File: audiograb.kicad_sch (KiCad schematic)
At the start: 4 parts, among them J2 USB_C_Receptacle_USB2.0_16P

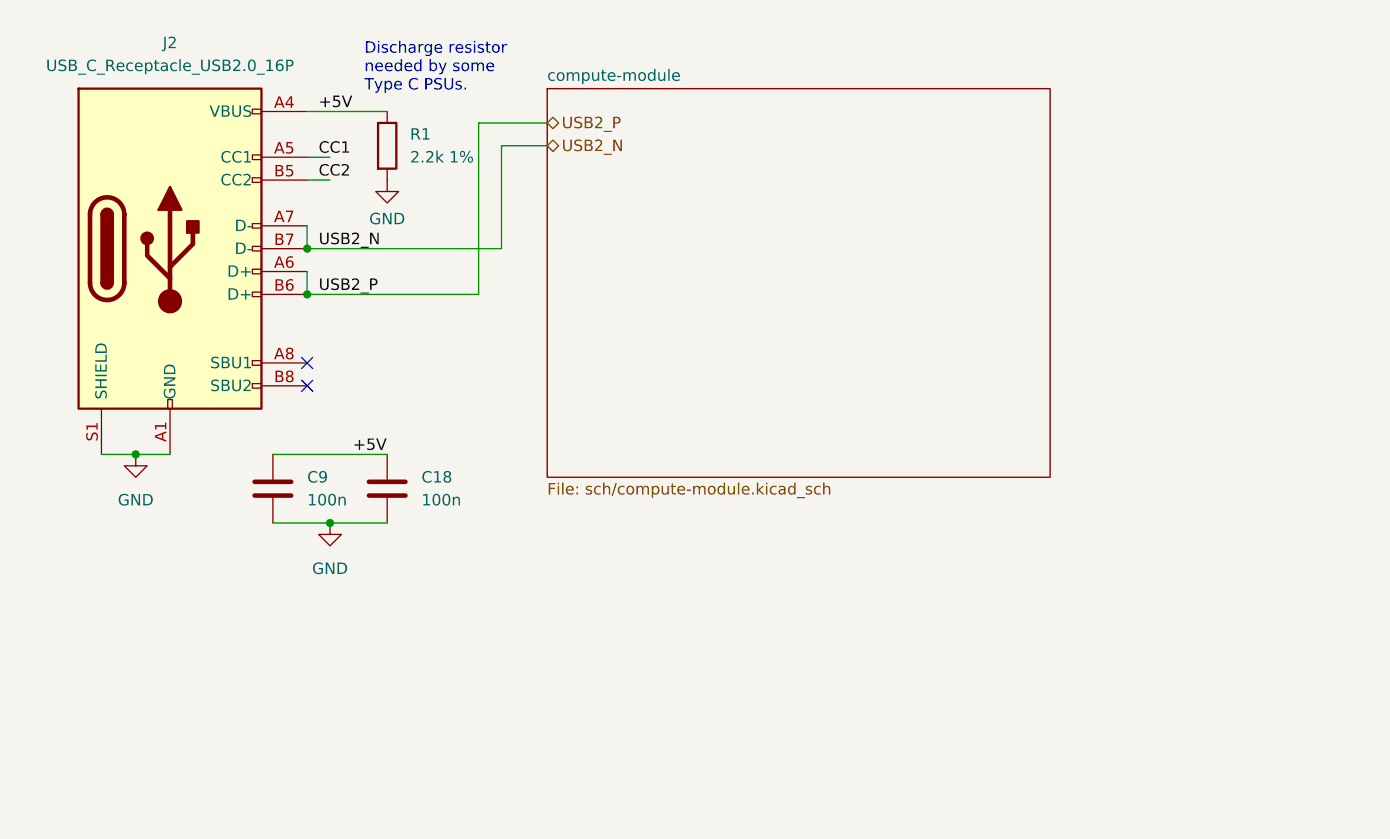
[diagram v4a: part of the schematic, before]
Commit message: compute module: added GPIO header, power, battery, among others
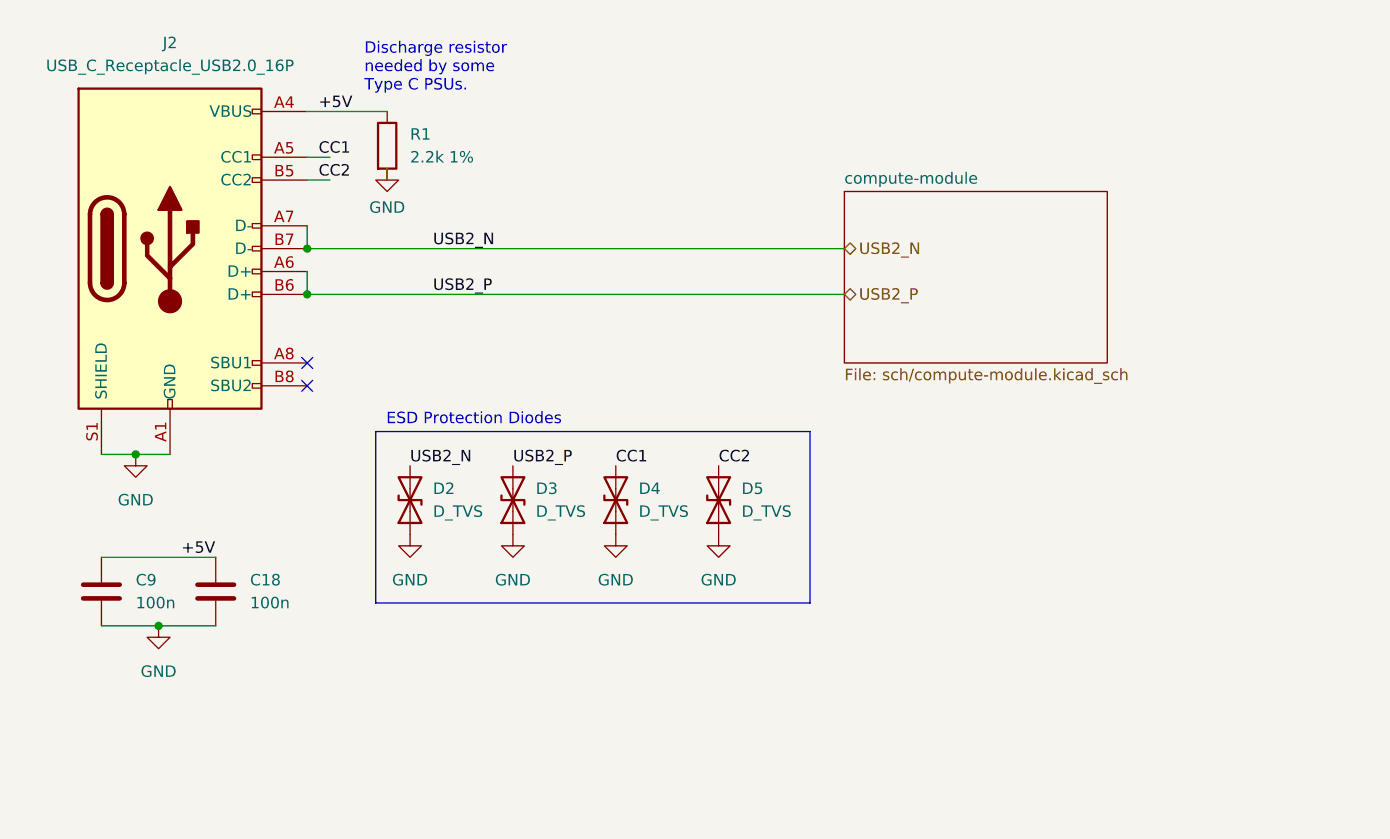
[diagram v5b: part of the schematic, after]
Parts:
- added D2, D3, D4, D5: D_TVS, symbol Device:D_TVS
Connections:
- net CC1: now also D4.2 (A2)
- net CC2: now also D5.2 (A2)
- net GND: now also D2.1 (A1), D3.1 (A1), D4.1 (A1), D5.1 (A1)
- net USB2_N: now also D2.2 (A2)
- net USB2_P: now also D3.2 (A2)
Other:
- note added: "ESD Protection Diodes"
- moved on the sheet: C18, C9

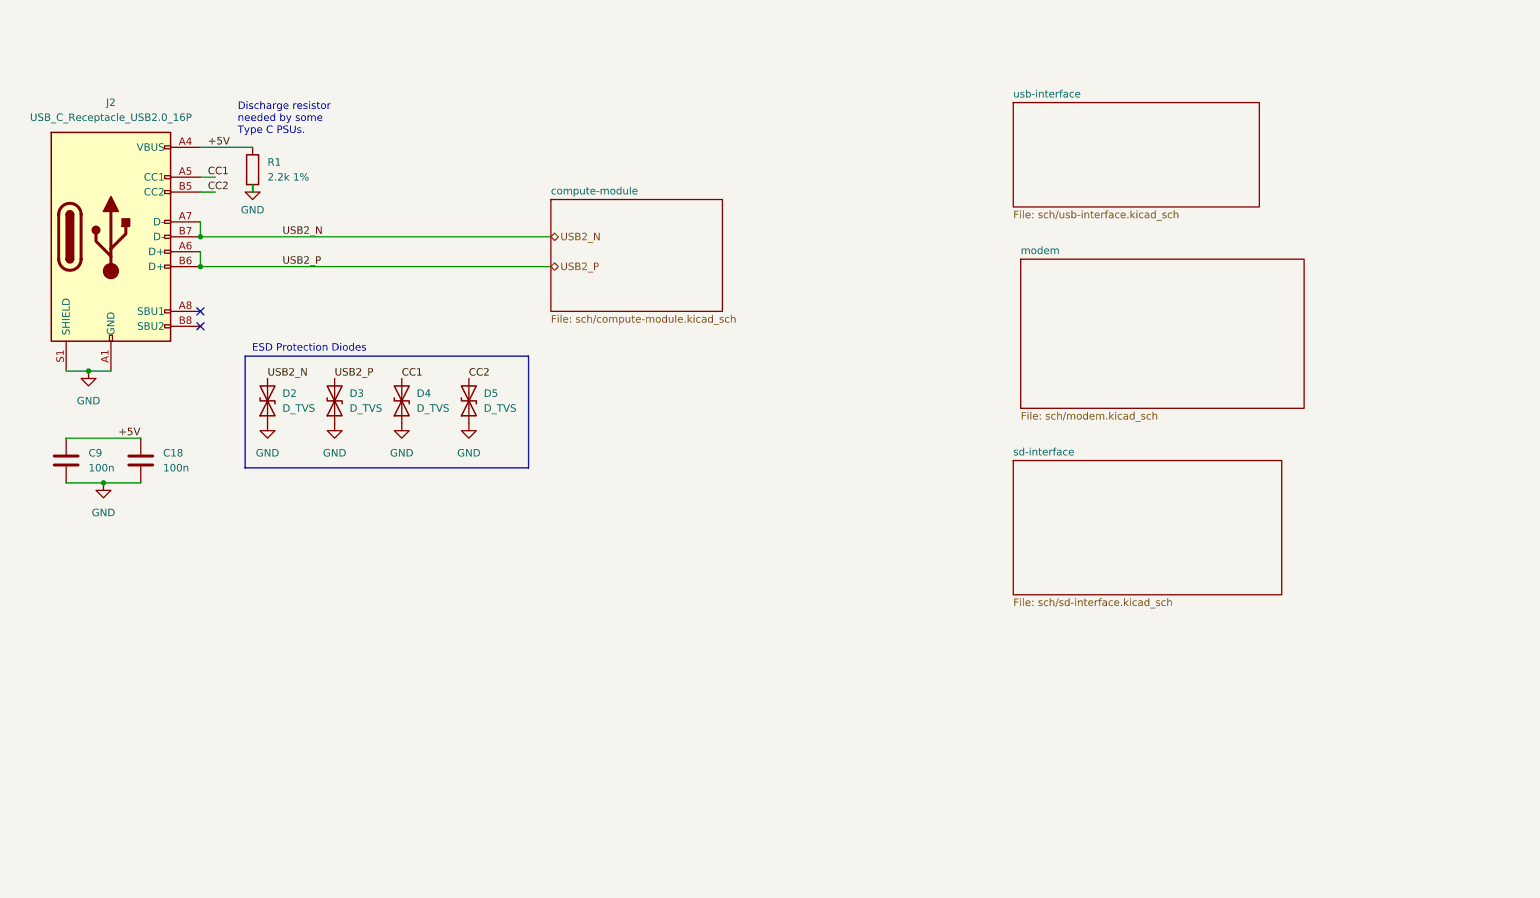
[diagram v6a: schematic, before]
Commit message: Added ports to CM5 and USB interface and connected them
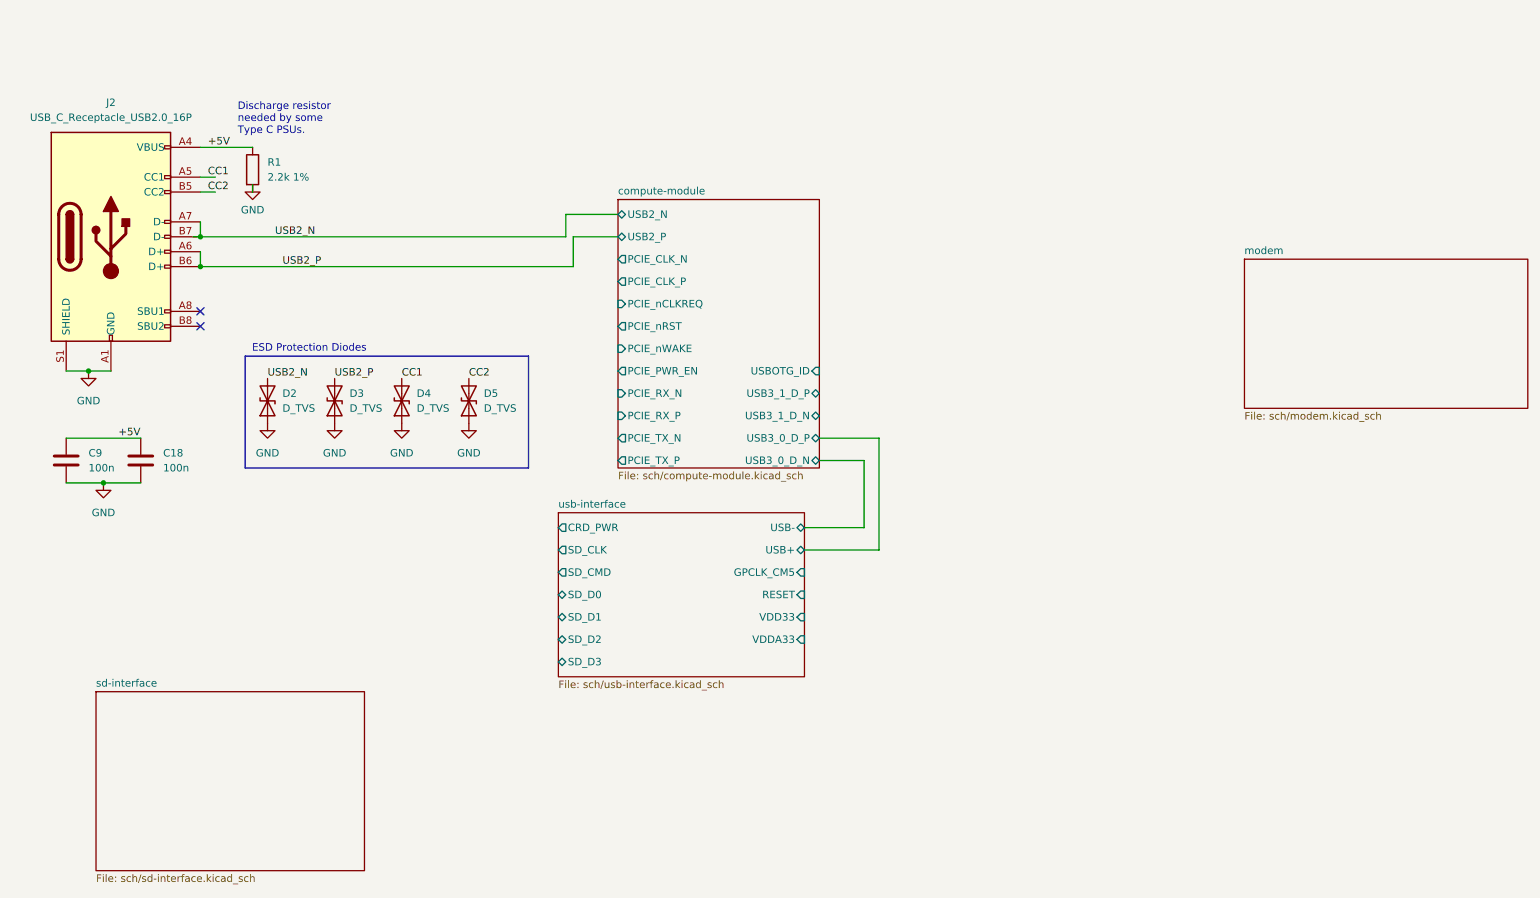
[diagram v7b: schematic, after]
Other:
- sheet compute-module ports: added PCIE_CLK_N, PCIE_CLK_P, PCIE_PWR_EN, PCIE_RX_N, PCIE_RX_P, PCIE_TX_N, PCIE_TX_P, PCIE_nCLKREQ, PCIE_nRST, PCIE_nWAKE, USB2_N, USB2_P, USB3_0_D_N, USB3_0_D_P, USB3_1_D_N, USB3_1_D_P, USBOTG_ID; removed none
- sheet usb-interface ports: added CRD_PWR, GPCLK_CM5, RESET, SD_CLK, SD_CMD, SD_D0, SD_D1, SD_D2, SD_D3, USB+, USB-, VDD33, VDDA33; removed none

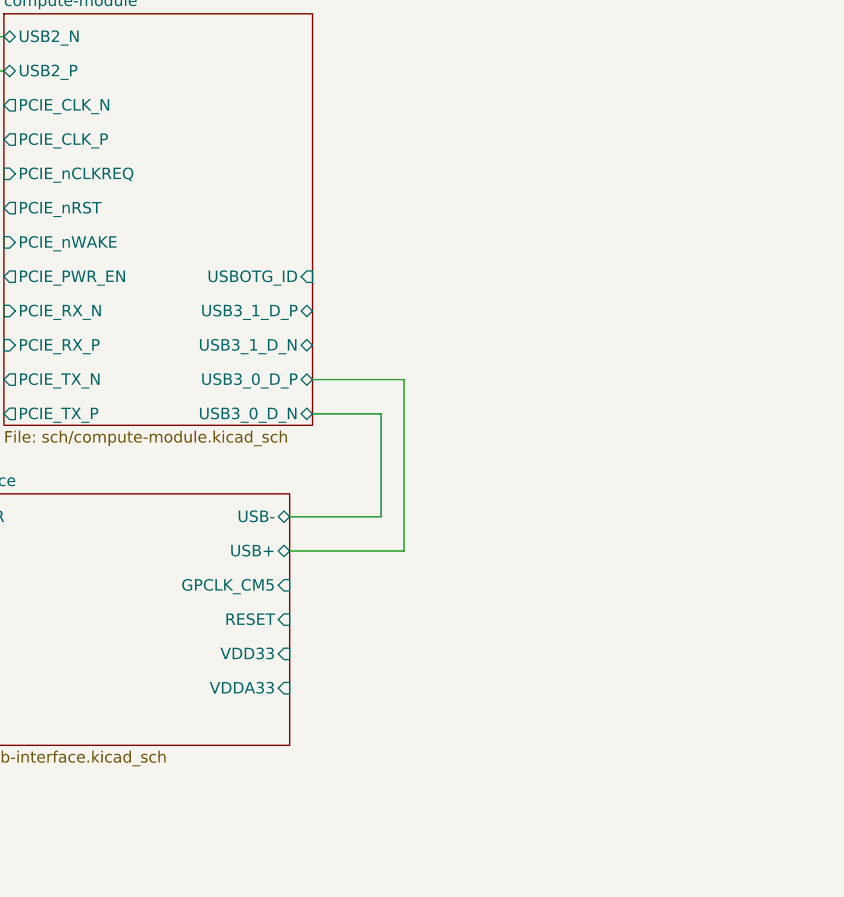
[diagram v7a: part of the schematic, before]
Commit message: Added more ports to the CM5 and connected them
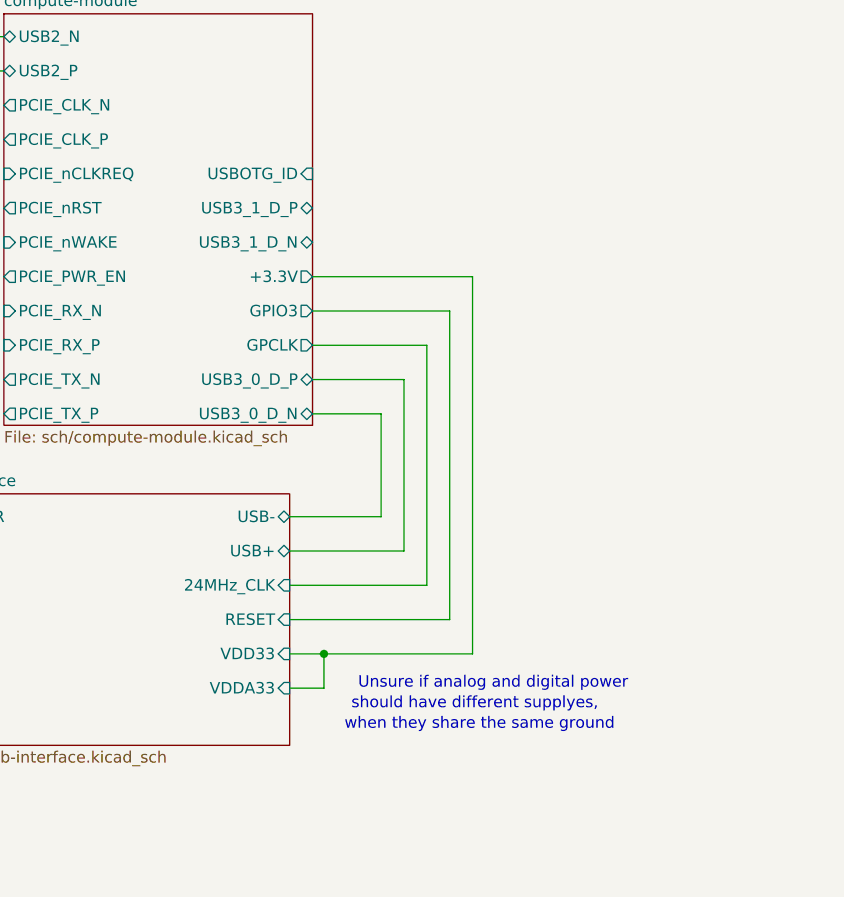
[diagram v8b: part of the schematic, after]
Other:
- sheet compute-module ports: added +3.3V, GPCLK, GPIO3; removed none
- sheet usb-interface ports: added 24MHz_CLK; removed GPCLK_CM5
- note added: "Unsure if analog and digital power"
- note added: "should have different supplyes,"
- note added: "when they share the same ground"
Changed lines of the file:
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@@
 		)
+	)
+	(text "should have different supplyes,"
+		(exclude_from_sim no)
+		(at 175.514 130.048 0)
+		(effects
+			(font
+				(size 1.27 1.27)
+			)
+		)
+	)
+	(text " when they share the same ground"
+		(exclude_from_sim no)
+		(at 175.768 132.334 0)
+		(effects
+			(font
+				(size 1.27 1.27)
+			)
+		)
+	)
+	(text "Unsure if analog and digital power "
+		(exclude_from_sim no)
+		(at 177.546 127.762 0)
+		(effects
+			(font
+				(size 1.27 1.27)
+			)
+		)
+	)
+	(junction
+		(at 158.75 124.46)
+		(diameter 0)
+		(color 0 0 0 0)
 	)
 	(junction
@@
 	(wire
 		(pts
+			(xy 158.75 124.46) (xy 158.75 128.27)
+		)
+		(stroke
+			(width 0)
+			(type default)
+		)
+	)
+	(wire
+		(pts
 			(xy 167.64 93.98) (xy 167.64 113.03)
 		)
@@
 	(wire
 		(pts
+			(xy 157.48 86.36) (xy 172.72 86.36)
+		)
+		(stroke
+			(width 0)
+			(type default)
+		)
+	)
+	(wire
+		(pts
 			(xy 50.8 59.69) (xy 52.07 59.69)
 		)
@@
 	(wire
 		(pts
+			(xy 154.94 120.65) (xy 172.72 120.65)
+		)
+		(stroke
+			(width 0)
+			(type default)
+		)
+	)
+	(wire
+		(pts
+			(xy 154.94 116.84) (xy 170.18 116.84)
+		)
+		(stroke
+			(width 0)
+			(type default)
+		)
+	)
+	(wire
+		(pts
+			(xy 157.48 82.55) (xy 175.26 82.55)
+		)
+		(stroke
+			(width 0)
+			(type default)
+		)
+	)
+	(wire
+		(pts
 			(xy 154.94 113.03) (xy 167.64 113.03)
 		)
@@
 	(wire
 		(pts
+			(xy 154.94 124.46) (xy 158.75 124.46)
+		)
+		(stroke
+			(width 0)
+			(type default)
+		)
+	)
+	(wire
+		(pts
 			(xy 52.07 44.45) (xy 60.96 44.45)
 		)
@@
 	(wire
 		(pts
+			(xy 170.18 90.17) (xy 170.18 116.84)
+		)
+		(stroke
+			(width 0)
+			(type default)
+		)
+	)
+	(wire
+		(pts
 			(xy 60.96 50.8) (xy 60.96 52.07)
 		)
@@
 	(wire
 		(pts
+			(xy 172.72 86.36) (xy 172.72 120.65)
+		)
+		(stroke
+			(width 0)
+			(type default)
+		)
+	)
+	(wire
+		(pts
 			(xy 33.02 82.55) (xy 36.83 82.55)
 		)
@@
 	(wire
 		(pts
+			(xy 158.75 124.46) (xy 175.26 124.46)
+		)
+		(stroke
+			(width 0)
+			(type default)
+		)
+	)
+	(wire
+		(pts
+			(xy 175.26 82.55) (xy 175.26 124.46)
+		)
+		(stroke
+			(width 0)
+			(type default)
+		)
+	)
+	(wire
+		(pts
 			(xy 52.07 57.15) (xy 52.07 59.69)
 		)
@@
 		(pts
 			(xy 114.3 55.88) (xy 123.19 55.88)
+		)
+		(stroke
+			(width 0)
+			(type default)
+		)
+	)
+	(wire
+		(pts
+			(xy 157.48 90.17) (xy 170.18 90.17)
+		)
+		(stroke
+			(width 0)
+			(type default)
+		)
+	)
+	(wire
+		(pts
+			(xy 154.94 128.27) (xy 158.75 128.27)
 		)
 		(stroke
@@
 			)
 		)
-		(pin "GPCLK_CM5" input
-			(at 154.94 116.84 0)
-			(effects
-				(font
-					(size 1.27 1.27)
-				)
-				(justify right)
-			)
-		)
 		(pin "RESET" input
 			(at 154.94 120.65 0)
@@
 		(pin "VDDA33" input
 			(at 154.94 128.27 0)
+			(effects
+				(font
+					(size 1.27 1.27)
+				)
+				(justify right)
+			)
+		)
+		(pin "24MHz_CLK" input
+			(at 154.94 116.84 0)
 			(effects
 				(font
@@
 		)
 		(pin "USB3_1_D_N" bidirectional
+			(at 157.48 78.74 0)
+			(effects
+				(font
+					(size 1.27 1.27)
+				)
+				(justify right)
+			)
+		)
+		(pin "USB3_1_D_P" bidirectional
+			(at 157.48 74.93 0)
+			(effects
+				(font
+					(size 1.27 1.27)
+				)
+				(justify right)
+			)
+		)
+		(pin "USBOTG_ID" input
+			(at 157.48 71.12 0)
+			(effects
+				(font
+					(size 1.27 1.27)
+				)
+				(justify right)
+			)
+		)
+		(pin "GPCLK" output
 			(at 157.48 90.17 0)
 			(effects
@@
 			)
 		)
-		(pin "USB3_1_D_P" bidirectional
+		(pin "GPIO3" output
 			(at 157.48 86.36 0)
 			(effects
@@
 			)
 		)
-		(pin "USBOTG_ID" input
+		(pin "+3.3V" output
 			(at 157.48 82.55 0)
 			(effects
